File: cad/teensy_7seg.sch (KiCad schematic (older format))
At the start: 17 parts, among them Q1 Q_NPN_EBC, Q2 Q_NPN_EBC, Q3 Q_NPN_EBC, Q4 Q_NPN_EBC, U1 Teensy3.1, U2 74HC595, U3 7-Seg_Bubble

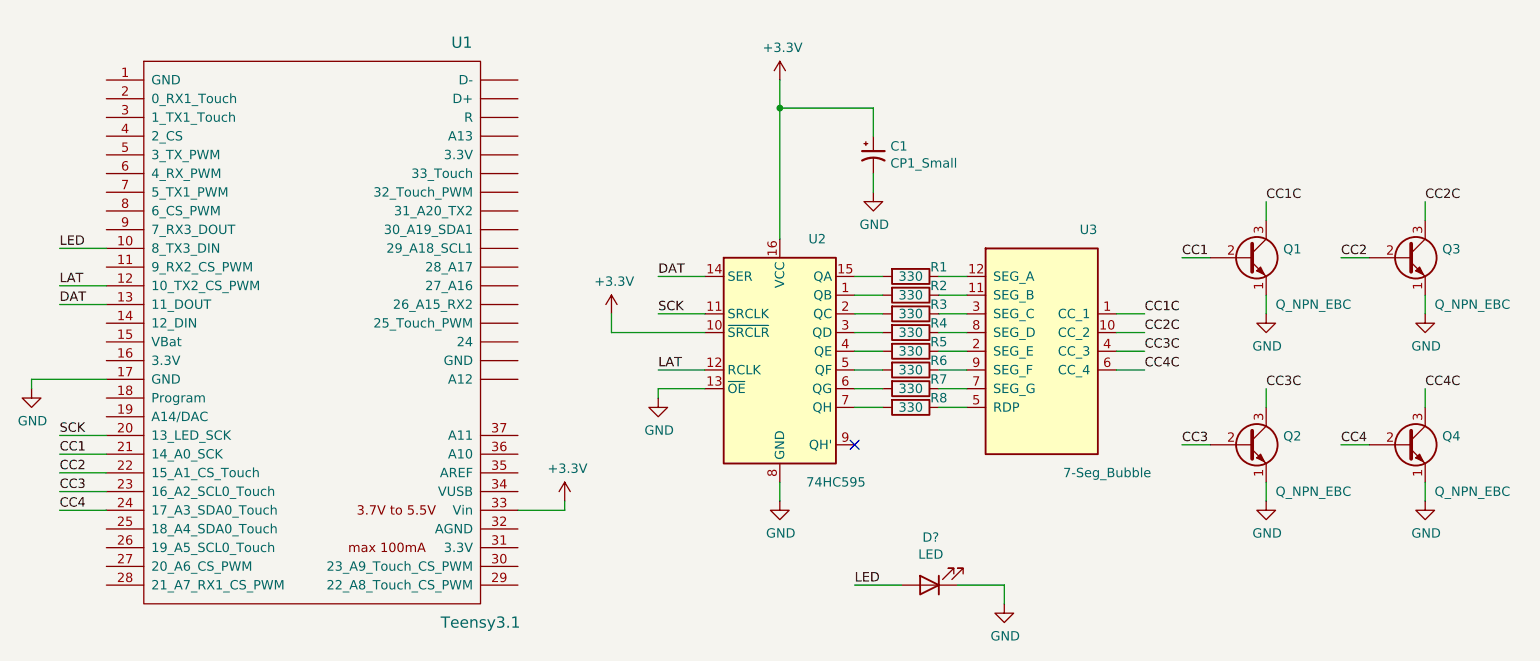
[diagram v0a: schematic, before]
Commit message: Adjusted CAD files
Re-arrangement and minor edits of KiCad files; no change to schematic design
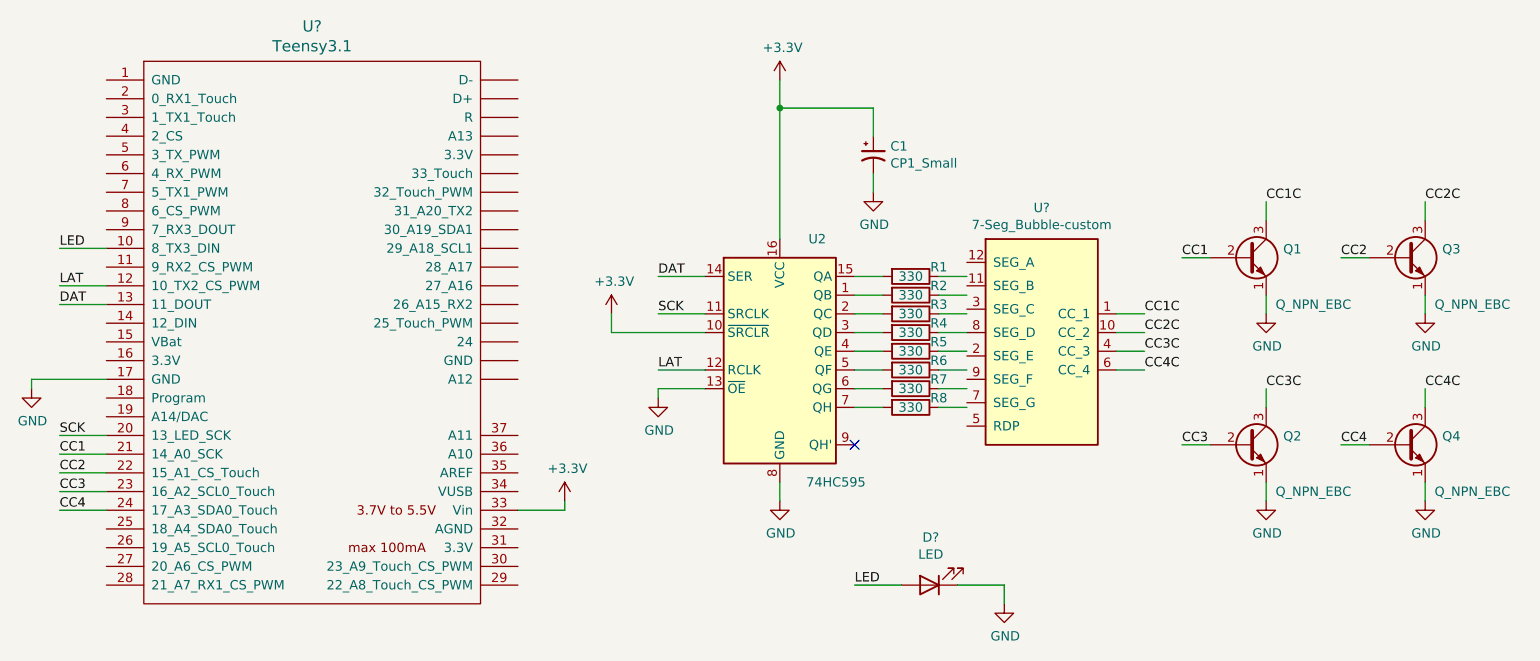
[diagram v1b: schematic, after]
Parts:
- removed U1: Teensy3.1, symbol teensy:Teensy3.1
- removed U3: 7-Seg_Bubble, symbol custom:7-Seg_Bubble
- added U?: Teensy3.1, symbol teensy:Teensy3.1
- added U?: 7-Seg_Bubble-custom, symbol custom:7-Seg_Bubble-custom
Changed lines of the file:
@@
 $EndDescr
-$Comp
-L teensy:Teensy3.1 U1
-U 1 1 5FD2FC87
-P 3550 4000
-F 0 "U1" H 4350 5550 60  0000 C CNN
-F 1 "Teensy3.1" H 4450 2450 60  0000 C CNN
-F 2 "" H 3550 3250 60  0000 C CNN
-F 3 "" H 3550 3250 60  0000 C CNN
-	1    3550 4000
-	1    0    0    -1
-$EndComp
 $Comp
 L 74xx:74HC595 U2
@@
 	1    6750 3700
 	0    1    1    0
-$EndComp
-$Comp
-L custom:7-Seg_Bubble U3
-U 1 1 5FD36AC2
-P 7450 4100
-F 0 "U3" H 7700 4750 50  0000 C CNN
-F 1 "7-Seg_Bubble" H 7800 3450 50  0000 C CNN
-F 2 "" H 7450 4100 50  0001 C CNN
-F 3 "" H 7450 4100 50  0001 C CNN
-	1    7450 4100
-	1    0    0    -1
 $EndComp
 $Comp
@@
 Wire Wire Line
 	7250 5350 7250 5450
+$Comp
+L teensy:Teensy3.1 U?
+U 1 1 61801CA4
+P 3550 4000
+F 0 "U?" H 3550 5637 60  0000 C CNN
+F 1 "Teensy3.1" H 3550 5531 60  0000 C CNN
+F 2 "" H 3550 3250 60  0000 C CNN
+F 3 "" H 3550 3250 60  0000 C CNN
+	1    3550 4000
+	1    0    0    -1
+$EndComp
+$Comp
+L custom:7-Seg_Bubble-custom U?
+U 1 1 61806A7B
+P 7450 4050
+F 0 "U?" H 7450 4767 50  0000 C CNN
+F 1 "7-Seg_Bubble-custom" H 7450 4676 50  0000 C CNN
+F 2 "" H 7450 4175 50  0001 C CNN
+F 3 "" H 7450 4175 50  0001 C CNN
+	1    7450 4050
+	1    0    0    -1
+$EndComp
 $EndSCHEMATC
